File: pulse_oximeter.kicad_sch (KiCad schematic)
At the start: 93 parts, among them SW1 B3F-1000, SW2 B3F-1000, SW3 B3F-1000, X1 Conn_01x03

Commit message: Посадочные места в библиотеке (GOST_FP), правила DRC «Резонит», отчёт по пунктам задания
Co-Authored-By: Claude Opus 5.5 <noreply@anthropic.com>
Claude-Session: https://claude.ai/code/session_01FsJMMwHQ3FuEgyASHhQBd4
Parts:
- C1, C10, C11, C12, C13, C14, C15, C16, C17, C18, C19, C2, C20, C21, C22, C23, C24, C25, C26, C27, C3, C33, C4, C49, C5, C6, C7, C8, C9: footprint Capacitor_THT:C_Disc_D5.1mm_W3.2mm_P5.00mm -> GOST_FP:C_Disc_D5.1mm_W3.2mm_P5.00mm
- DA1, DA2, DA3, DA4, DA5, DA6, DA7: footprint Package_DIP:DIP-8_W7.62mm -> GOST_FP:DIP-8_W7.62mm
- DA8: footprint Package_DIP:DIP-16_W7.62mm -> GOST_FP:DIP-16_W7.62mm
- DA9: footprint Package_TO_SOT_SMD:SOT-223-3_TabPin2 -> GOST_FP:SOT-223-3_TabPin2
- DD1: footprint Package_QFP:LQFP-48_7x7mm_P0.5mm -> GOST_FP:LQFP-48_7x7mm_P0.5mm
- DD2: footprint Package_SO:SSOP-28_5.3x10.2mm_P0.65mm -> GOST_FP:SSOP-28_5.3x10.2mm_P0.65mm
- HL1, HL2: footprint OptoDevice:LaserDiode_TO18-D5.6-3 -> GOST_FP:LaserDiode_TO18-D5.6-3
- R1, R11, R12, R18, R21, R23, R28, R4, R5, R6, R62, R7: footprint Resistor_THT:R_Axial_DIN0309_L9.0mm_D3.2mm_P2.54mm_Vertical -> GOST_FP:R_Axial_DIN0309_L9.0mm_D3.2mm_P2.54mm_Vertical; Manufacturer_Part_Number MFR-50FBF52-10K -> MFR50SFTE52-10K
- R10, R16, R17, R2, R22, R3, R35, R40, R9: footprint Resistor_THT:R_Axial_DIN0309_L9.0mm_D3.2mm_P2.54mm_Vertical -> GOST_FP:R_Axial_DIN0309_L9.0mm_D3.2mm_P2.54mm_Vertical; Manufacturer_Part_Number MFR-50FBF52-22K -> MFR50SFTE52-22K
- R13, R19, R20, R29, R37, R44: footprint Potentiometer_THT:Potentiometer_Bourns_3296W_Vertical -> GOST_FP:Potentiometer_Bourns_3296W_Vertical
- R14, R24, R25, R27, R30, R31, R42, R63, R8: footprint Resistor_THT:R_Axial_DIN0309_L9.0mm_D3.2mm_P2.54mm_Vertical -> GOST_FP:R_Axial_DIN0309_L9.0mm_D3.2mm_P2.54mm_Vertical; Manufacturer_Part_Number MFR-50FBF52-390R -> MFR50SFTE52-390R
- R15, R26, R34, R43: footprint Resistor_THT:R_Axial_DIN0309_L9.0mm_D3.2mm_P2.54mm_Vertical -> GOST_FP:R_Axial_DIN0309_L9.0mm_D3.2mm_P2.54mm_Vertical; Manufacturer_Part_Number MFR-50FBF52-2K2 -> MFR50SFTE52-2K2
- SW1, SW2, SW3: footprint Button_Switch_THT:SW_PUSH_6mm -> GOST_FP:SW_PUSH_6mm
- VD1: footprint OptoDevice:Osram_DIL2_4.3x4.65mm_P5.08mm -> GOST_FP:Osram_DIL2_4.3x4.65mm_P5.08mm
- VD2, VD3, VD4, VD5: footprint Diode_THT:D_DO-41_SOD81_P10.16mm_Horizontal -> GOST_FP:D_DO-41_SOD81_P10.16mm_Horizontal
- VT1, VT2: footprint Package_TO_SOT_THT:TO-126-3_Vertical -> GOST_FP:TO-126-3_Vertical
- X1: footprint Connector_PinHeader_2.54mm:PinHeader_1x03_P2.54mm_Vertical -> GOST_FP:PinHeader_1x03_P2.54mm_Vertical

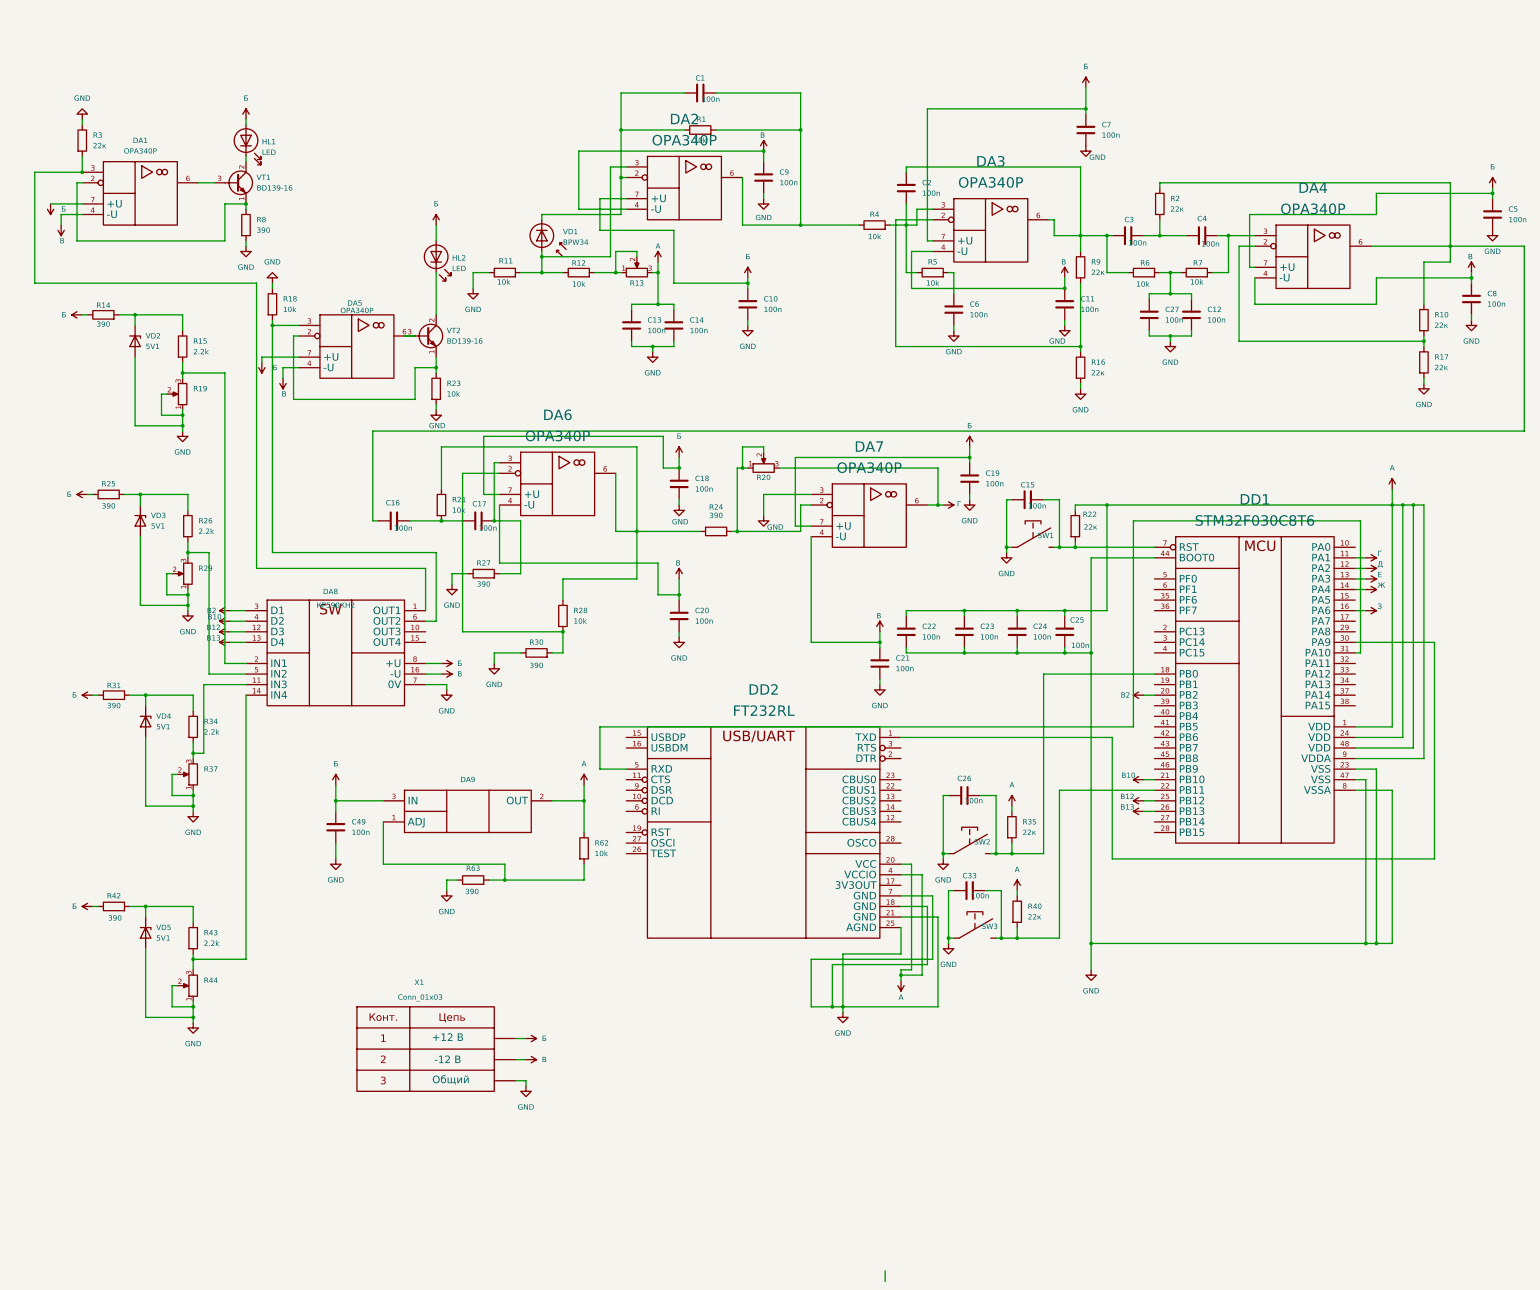
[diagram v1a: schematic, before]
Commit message: Схема переведена на ГОСТ-УГО (R, C, подстроечные, светодиоды, фотодиод, стабилитроны, транзисторы, общий провод); метки основных цепей; классы цепей по меткам
Co-Authored-By: Claude Opus 5.5 <noreply@anthropic.com>
Claude-Session: https://claude.ai/code/session_01FsJMMwHQ3FuEgyASHhQBd4
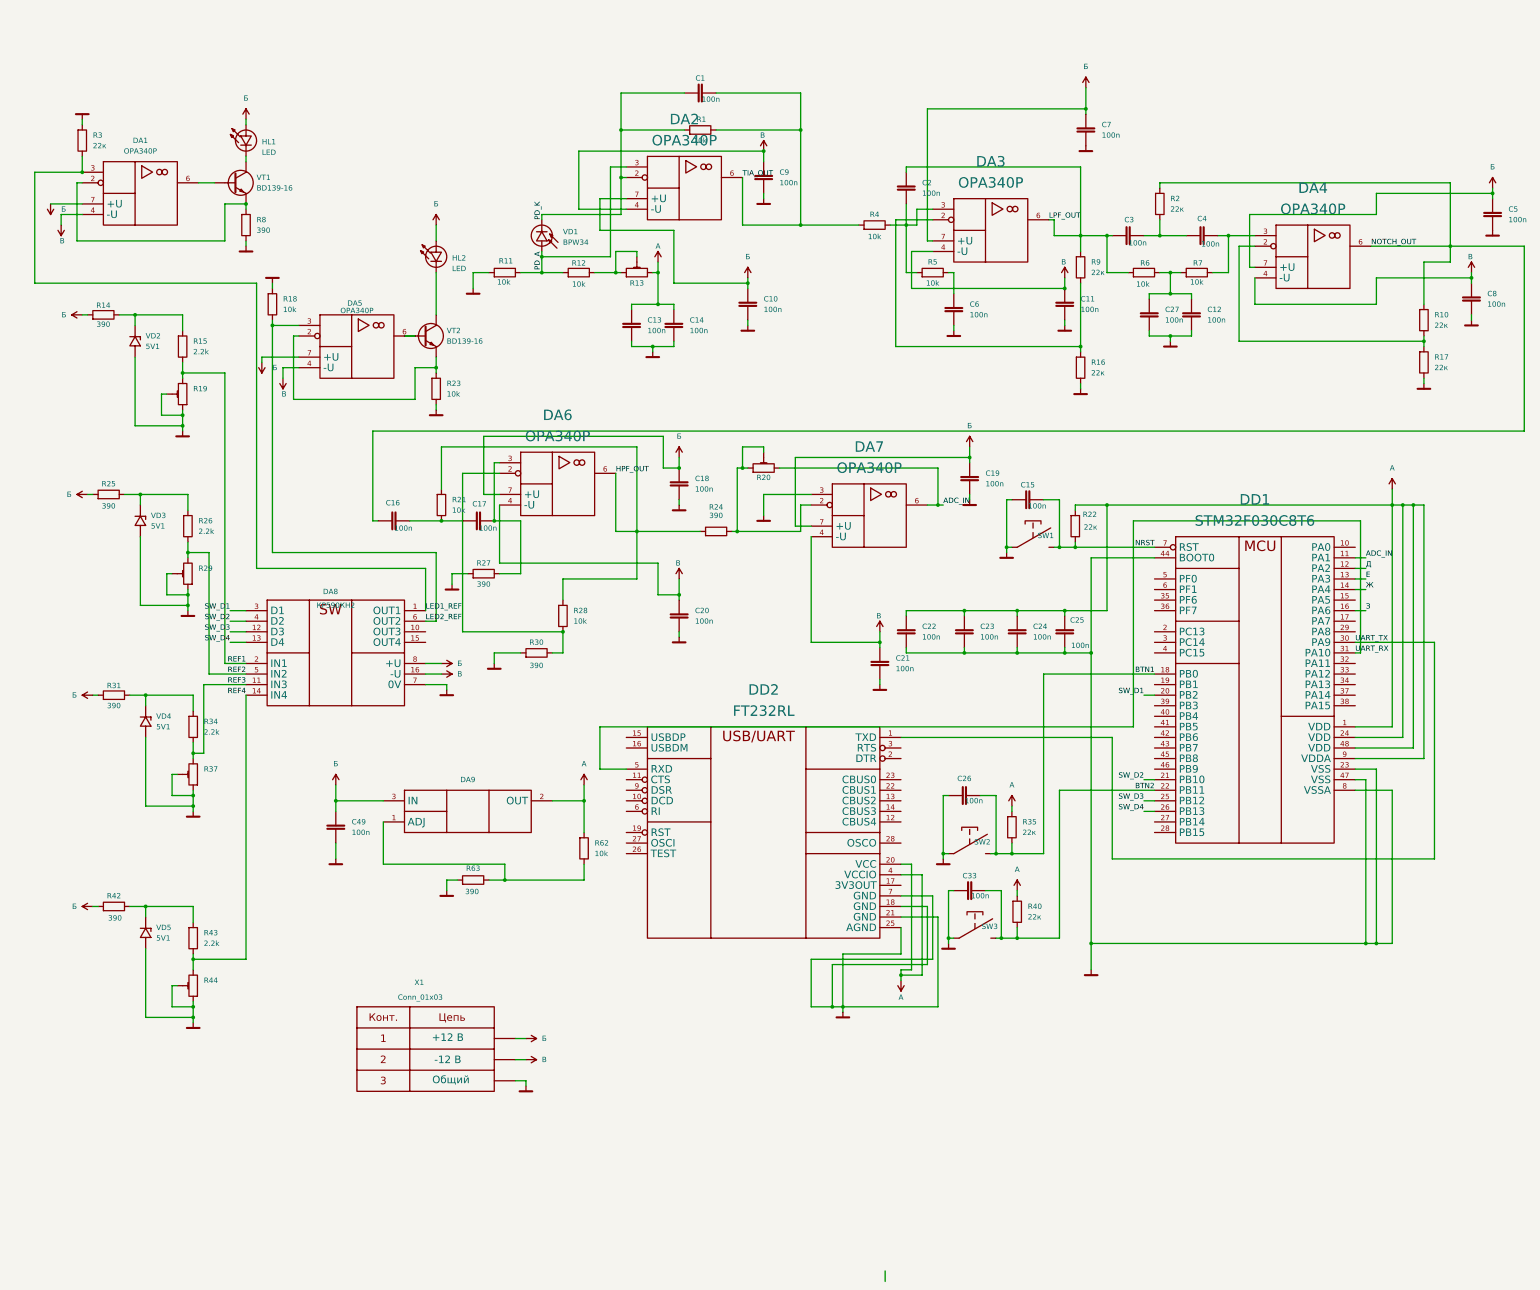
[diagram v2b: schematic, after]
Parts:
- C1, C10, C11, C12, C13, C14, C15, C16, C17, C18, C19, C2, C20, C21, C22, C23, C24, C25, C26, C27, C3, C33, C4, C49, C5, C6, C7, C8, C9: symbol Device:C -> GOST_UGO:C
- HL1, HL2: symbol Device:LED -> GOST_UGO:LED
- R1, R10, R11, R12, R14, R15, R16, R17, R18, R2, R21, R22, R23, R24, R25, R26, R27, R28, R3, R30, R31, R34, R35, R4, R40, R42, R43, R5, R6, R62, R63, R7, R8, R9: symbol Device:R -> GOST_UGO:R
- R13, R19, R20, R29, R37, R44: symbol Device:R_Potentiometer -> GOST_UGO:R_Trim
- VD1: symbol Sensor_Optical:BPW34 -> GOST_UGO:Photodiode
- VD2, VD3, VD4, VD5: symbol Diode:ZYxxx -> GOST_UGO:D_Zener
- VT1, VT2: symbol Transistor_BJT:BD235 -> GOST_UGO:Q_NPN
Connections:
- net BTN1: now reaches C26.2, DD1.18 (PB0), R35.2, SW2.2
- net PD_K: now reaches C1.1, DA2.2, R1.1, VD1.1 (K)
- net PD_A: now reaches DA2.3, R11.2, R12.1, VD1.2 (A)
- net REF4: now reaches DA8.14 (IN4), R43.2, R44.3
- net NOTCH_OUT: now reaches C16.1, DA4.6, R10.1, R2.1
- net BTN2: now reaches C33.2, DD1.22 (PB11), R40.2, SW3.2
- net UART_TX: now reaches DD1.30 (PA9), DD2.1 (TXD)
- net UART_RX: now reaches DD1.31 (PA10), DD2.5 (RXD)
- net NRST: now reaches C15.2, DD1.7 (RST), R22.2, SW1.2
- net HPF_OUT: now reaches DA6.6, R21.1, R24.1, R28.1
- net REF1: now reaches DA8.2 (IN1), R15.2, R19.3
- net TIA_OUT: now reaches C1.2, DA2.6, R1.2, R4.1
- net LPF_OUT: now reaches C2.2, C3.1, DA3.6, R6.1, R9.1
- net REF3: now reaches DA8.11 (IN3), R34.2, R37.3
- net LED1_REF: now reaches DA1.3, DA8.1 (OUT1), R3.2
- net REF2: now reaches DA8.5 (IN2), R26.2, R29.3
- net LED2_REF: now reaches DA5.3, DA8.6 (OUT2), R18.2
- net В10 renamed SW_D2
- net В12 renamed SW_D3
- net В13 renamed SW_D4
- net В2 renamed SW_D1
- net Г renamed ADC_IN

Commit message: Итоговая версия проекта: схема и плата после трассировки, все УГО и посадочные места из библиотеки, ERC/DRC без ошибок, STEP в скрипте, отчёт обновлён
Co-Authored-By: Claude Opus 5.5 <noreply@anthropic.com>
Claude-Session: https://claude.ai/code/session_01FsJMMwHQ3FuEgyASHhQBd4
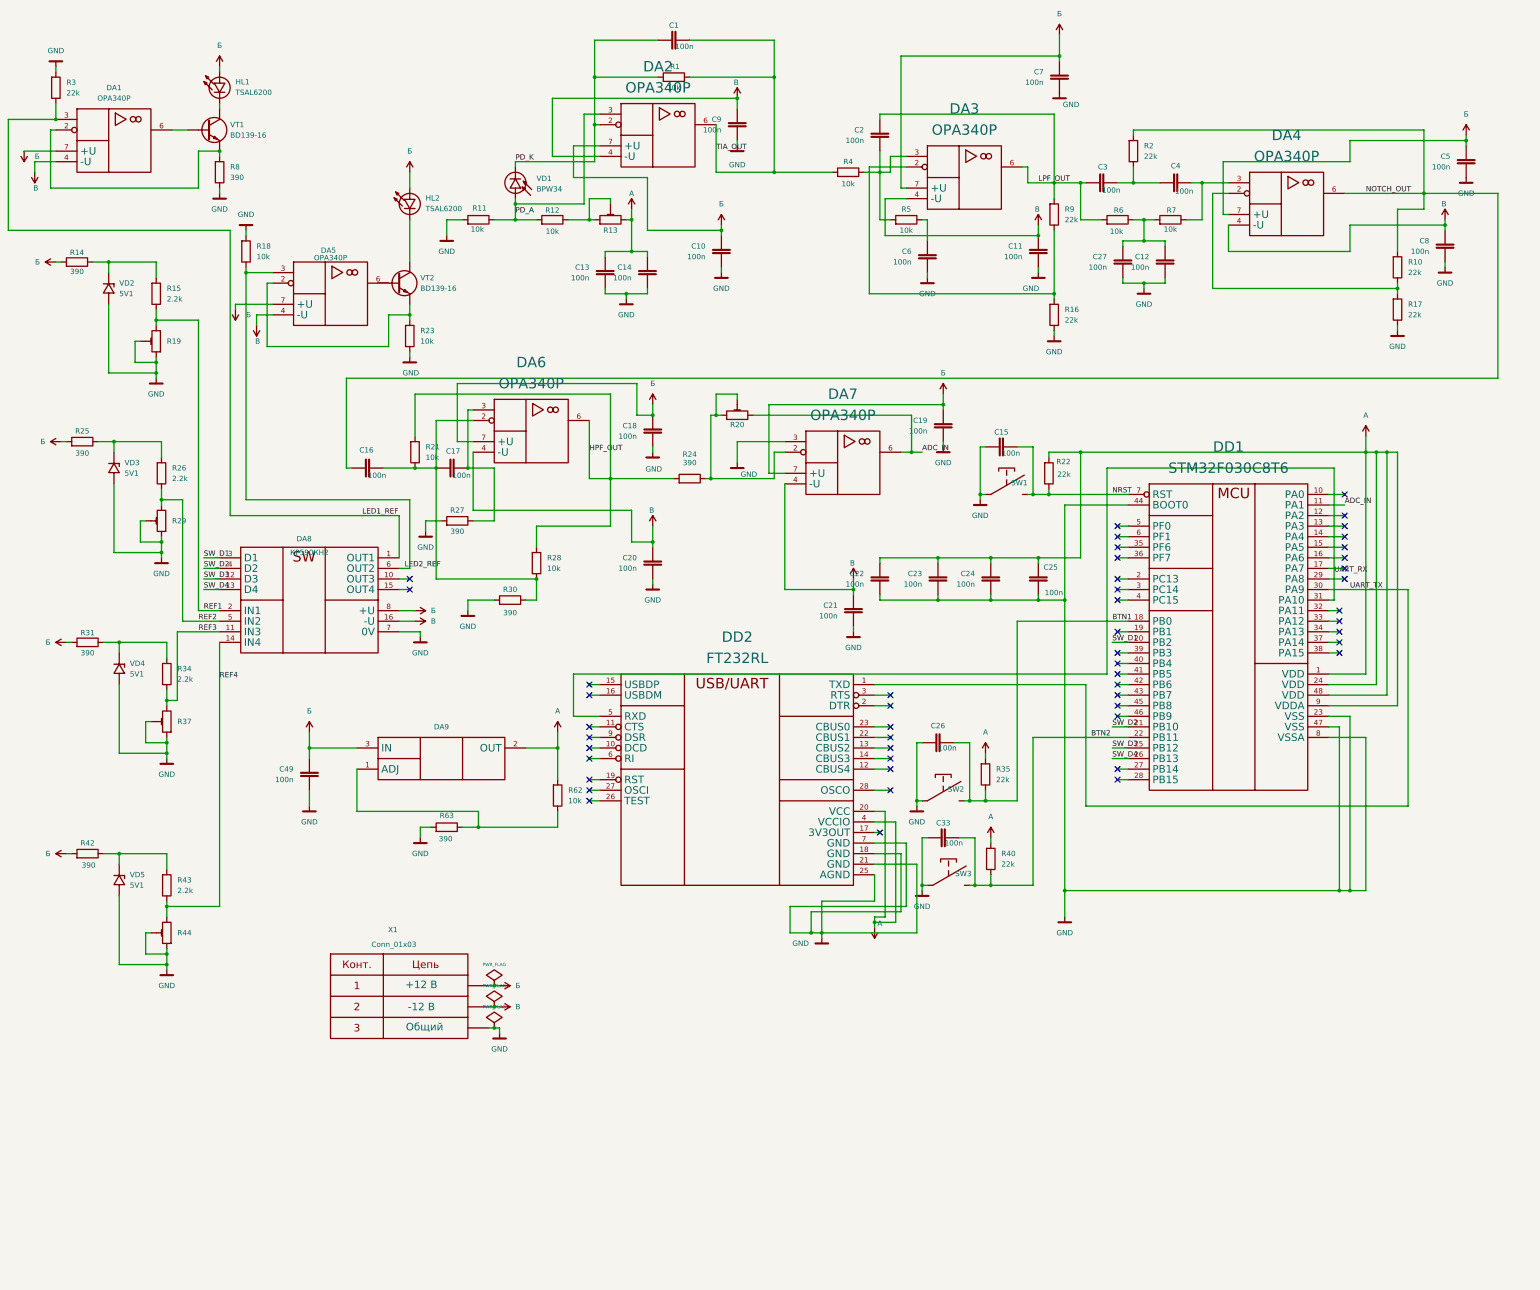
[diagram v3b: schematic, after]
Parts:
- DA9: value LM1117MP-ADJ -> LM1117T-ADJ; footprint GOST_FP:SOT-223-3_TabPin2 -> GOST_FP:TO-220-3_Vertical; Manufacturer_Part_Number LM1117MPX-ADJ/NOPB -> LM1117T-ADJ/NOPB
- HL1, HL2: value LED -> TSAL6200
- R10, R16, R17, R2, R22, R3, R35, R40, R9: value 22к -> 22k
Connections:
- net at DA6.2, R28.2, R30.2: now also C16.2, C17.1, R21.2
- net Д: no longer names the net of DD1.12 (PA2)
- net Е: no longer names the net of DD1.13 (PA3)
- net Ж: no longer names the net of DD1.14 (PA4)
- net З: no longer names the net of DD1.16 (PA6)
- no-connect marks 0 -> 50
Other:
- moved on the sheet: C1, C10, C11, C12, C13, C14, C15, C16, C17, C18, C19, C2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
